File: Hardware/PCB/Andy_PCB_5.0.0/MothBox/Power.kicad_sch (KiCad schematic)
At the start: 28 parts, among them P1 Raw Input, P2 12V Regulated Input, P3 Input to regulator, Q1 BC817, Q2 TJ10S04M3L,LXHQ, U15 Place Holder voltage regulator, U19 INA219BIDCNT, U3 XL4015E1

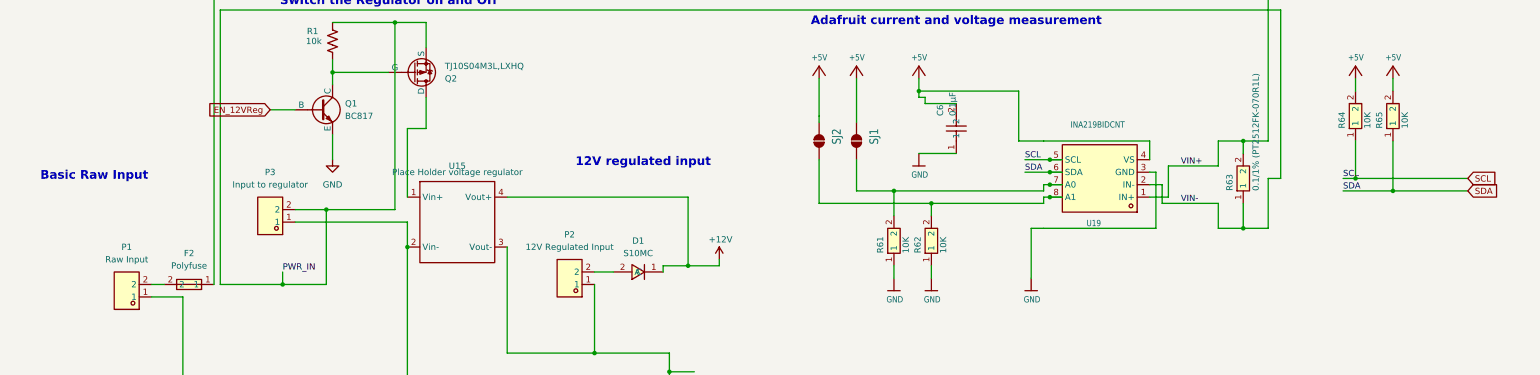
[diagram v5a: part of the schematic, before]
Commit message: added GPS 2 kinds
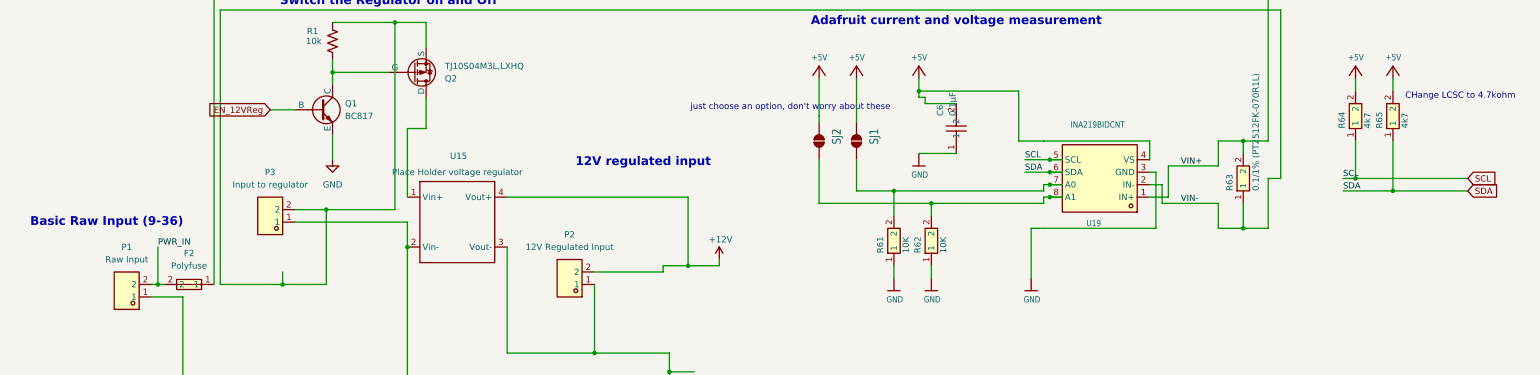
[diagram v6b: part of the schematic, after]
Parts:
- removed D1: S10MC, easyeda2kicad:SMC_L7.1-W6.2-LS8.1-RD, symbol easyeda2kicad:S10MC
- R64, R65: value 10K -> 4k7
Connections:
- net +12V: now also P2.2
- net PWR_IN: now also F2.2, P1.2; no longer P3.2, Q2.3 (S), R1.2, R63.1, U19.2 (IN-)
- new net VIN-: P3.2, Q2.3 (S), R1.2, R63.1, U19.2 (IN-)
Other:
- note added: "Basic Raw Input (9-36)"
- note added: "CHange LCSC to 4.7kohm"
- note added: "just choose an option, don't worry about these"
- note removed: "Basic Raw Input"
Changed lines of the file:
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@@
 		)
 	)
+	(text "CHange LCSC to 4.7kohm\n"
+		(exclude_from_sim no)
+		(at 317.246 35.306 0)
+		(effects
+			(font
+				(size 1.27 1.27)
+			)
+		)
+	)
+	(text "just choose an option, don't worry about these\n"
+		(exclude_from_sim no)
+		(at 180.848 37.592 0)
+		(effects
+			(font
+				(size 1.27 1.27)
+			)
+		)
+	)
 	(text "12V regulated input\n"
 		(exclude_from_sim no)
@@
 		)
 	)
-	(text "Basic Raw Input"
+	(text "Basic Raw Input (9-36)"
 		(exclude_from_sim no)
-		(at 39.116 51.562 0)
+		(at 41.656 60.96 0)
 		(effects
 			(font
@@
 	)
 	(junction
+		(at 52.07 73.66)
+		(diameter 0)
+		(color 0 0 0 0)
+	)
+	(junction
 		(at 140.97 87.63)
 		(diameter 0)
@@
 	(wire
 		(pts
+			(xy 50.8 73.66) (xy 52.07 73.66)
+		)
+		(stroke
+			(width 0)
+			(type default)
+		)
+	)
+	(wire
+		(pts
 			(xy 64.77 130.81) (xy 73.66 130.81)
 		)
@@
 	(wire
 		(pts
+			(xy 52.07 66.04) (xy 52.07 73.66)
+		)
+		(stroke
+			(width 0)
+			(type default)
+		)
+	)
+	(wire
+		(pts
 			(xy 254 55.88) (xy 257.81 55.88)
 		)
@@
 	(wire
 		(pts
-			(xy 140.97 71.12) (xy 144.78 71.12)
+			(xy 140.97 71.12) (xy 154.94 71.12)
 		)
 		(stroke
@@
 	(wire
 		(pts
-			(xy 50.8 73.66) (xy 53.34 73.66)
-		)
-		(stroke
-			(width 0)
-			(type default)
-		)
-	)
-	(wire
-		(pts
 			(xy 87.63 30.48) (xy 99.06 30.48)
 		)
@@
 	(wire
 		(pts
+			(xy 52.07 73.66) (xy 53.34 73.66)
+		)
+		(stroke
+			(width 0)
+			(type default)
+		)
+	)
+	(wire
+		(pts
 			(xy 146.05 128.27) (xy 146.05 120.65)
 		)
@@
 		)
 	)
-	(label "PWR_IN"
-		(at 77.47 71.12 0)
+	(label "FB"
+		(at 144.78 133.35 0)
 		(effects
 			(font
@@
 		)
 	)
-	(label "FB"
-		(at 144.78 133.35 0)
+	(label "SDA"
+		(at 228.6 50.8 0)
 		(effects
 			(font
-				(size 1.27 1.27)
+				(size 1.2446 1.2446)
 			)
 			(justify left bottom)
 		)
 	)
-	(label "SDA"
-		(at 228.6 50.8 0)
+	(label "PWR_IN"
+		(at 52.07 66.04 0)
 		(effects
 			(font
-				(size 1.2446 1.2446)
+				(size 1.27 1.27)
 			)
 			(justify left bottom)
@@
 			)
 		)
-		(property "Value" "10K"
+		(property "Value" "4k7"
 			(at 299.085 41.91 0)
 			(effects
@@
 	)
 	(symbol
-		(lib_id "easyeda2kicad:S10MC")
-		(at 149.86 71.12 180)
-		(unit 1)
-		(exclude_from_sim no)
-		(in_bom yes)
-		(on_board yes)
-		(dnp no)
-		(fields_autoplaced yes)
-		(property "Reference" "D1"
-			(at 149.86 64.77 0)
-			(effects
-				(font
-					(size 1.27 1.27)
-				)
-			)
-		)
-		(property "Value" "S10MC"
-			(at 149.86 67.31 0)
-			(effects
-				(font
-					(size 1.27 1.27)
-				)
-			)
-		)
-		(property "Footprint" "easyeda2kicad:SMC_L7.1-W6.2-LS8.1-RD"
-			(at 149.86 63.5 0)
-			(effects
-				(font
-					(size 1.27 1.27)
-				)
-				(hide yes)
-			)
-		)
-		(property "Datasheet" "https://lcsc.com/product-detail/Diodes-General-Purpose_S10MC_C169472.html"
-			(at 149.86 60.96 0)
-			(effects
-				(font
-					(size 1.27 1.27)
-				)
-				(hide yes)
-			)
-		)
-		(property "Description" ""
-			(at 149.86 71.12 0)
-			(effects
-				(font
-					(size 1.27 1.27)
-				)
-				(hide yes)
-			)
-		)
-		(property "LCSC Part" "C169472"
-			(at 149.86 58.42 0)
-			(effects
-				(font
-					(size 1.27 1.27)
-				)
-				(hide yes)
-			)
-		)
-		(pin "1"
-		)
-		(pin "2"
-		)
-		(instances
-			(project ""
-				(path "/9021e528-fc76-4423-a3f3-30f5652071cc/4a573100-9946-48c2-8ae5-35f893607623"
-					(reference "D1")
-					(unit 1)
-				)
-			)
-		)
-	)
-	(symbol
 		(lib_id "New_Library:Buck-Boost")
 		(at 113.03 60.96 0)
@@
 		(on_board no)
 		(dnp no)
-		(fields_autoplaced yes)
 		(property "Reference" "U15"
-			(at 113.03 49.53 0)
+			(at 113.284 47.498 0)
 			(effects
 				(font
@@
 			)
 		)
-		(property "Value" "10K"
+		(property "Value" "4k7"
 			(at 306.705 41.91 0)
 			(effects

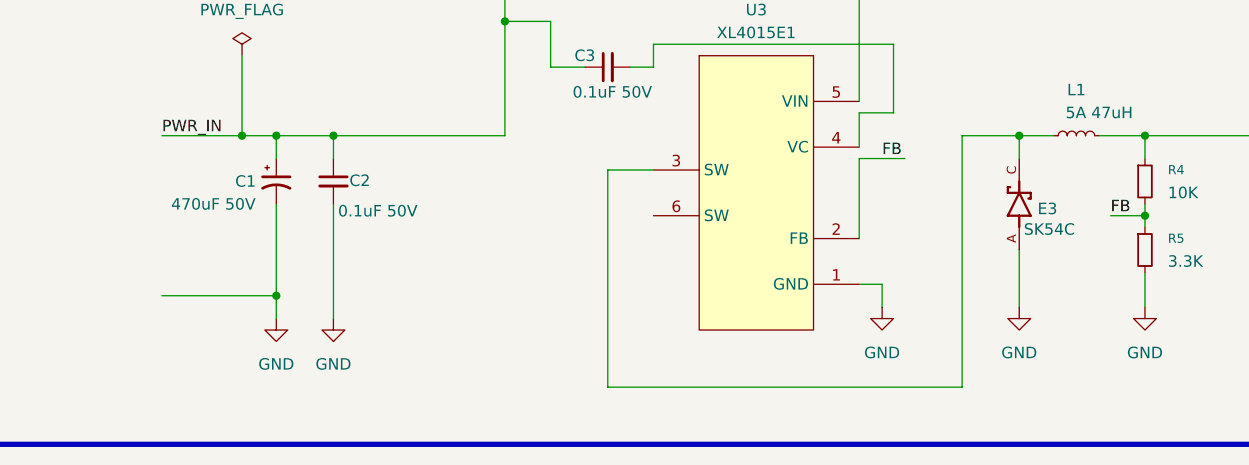
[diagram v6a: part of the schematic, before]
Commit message: Tweaked Mothbeam and added GPS footprints
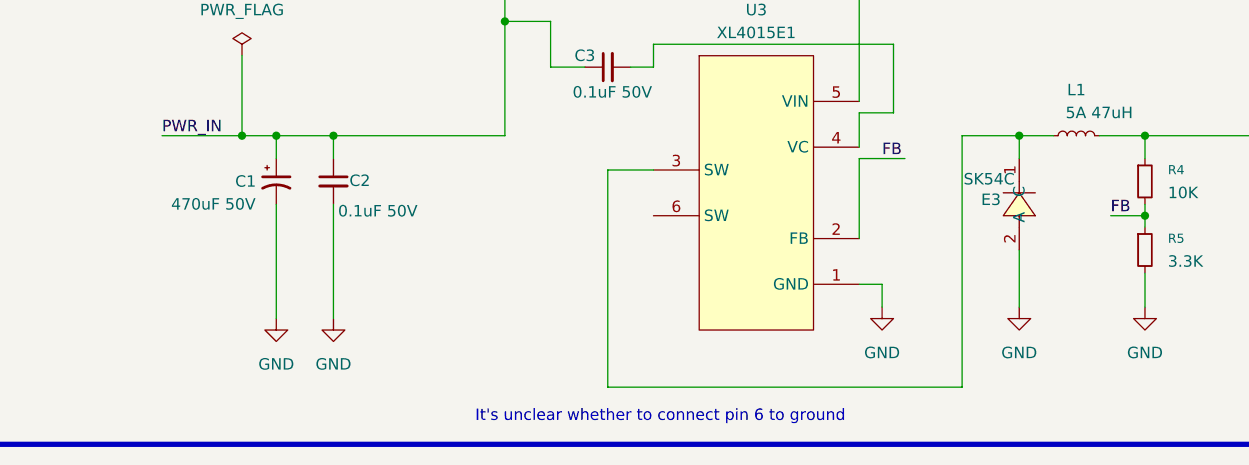
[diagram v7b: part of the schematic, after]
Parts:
- E3: footprint SK54C:DIO_SK54C -> easyeda2kicad:SMC_L6.9-W5.9-LS8.0-RD; symbol SK54C:SK54C -> easyeda2kicad:SK54C_C5449119; LCSC Part (none) -> C5449119
- P1, P2, P3: footprint easyeda2kicad:CONN-TH_DB301V-3.5-2P-GN -> easyeda2kicad:CONN-TH_2P-P5.08_DIBO_DB142R-5.08-2P; symbol easyeda2kicad:DB301V-3.5-2P-GN -> easyeda2kicad:DB142R-5.08-2P; LCSC Part C695629 -> C2898709
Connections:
- net GND: now also E3.2 (A); no longer E3.A
- net at L1.1, U3.3 (SW): now also E3.1 (C); no longer E3.C
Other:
- note added: "It's unclear whether to connect pin 6 to ground"
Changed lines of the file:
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@@
 		)
 	)
+	(text "It's unclear whether to connect pin 6 to ground\n"
+		(exclude_from_sim no)
+		(at 120.142 162.052 0)
+		(effects
+			(font
+				(size 1.27 1.27)
+				(color 255 20 18 1)
+			)
+		)
+	)
 	(text "CHange LCSC to 4.7kohm\n"
 		(exclude_from_sim no)
@@
 	)
 	(junction
-		(at 77.47 148.59)
-		(diameter 0)
-		(color 0 0 0 0)
-	)
-	(junction
 		(at 233.68 50.8)
 		(diameter 0)
@@
 	(wire
 		(pts
-			(xy 64.77 148.59) (xy 77.47 148.59)
-		)
-		(stroke
-			(width 0)
-			(type default)
-		)
-	)
-	(wire
-		(pts
 			(xy 278.13 13.97) (xy 278.13 44.45)
 		)
@@
 	(wire
 		(pts
-			(xy 77.47 138.43) (xy 77.47 148.59)
+			(xy 77.47 138.43) (xy 77.47 151.13)
 		)
 		(stroke
@@
 	(wire
 		(pts
-			(xy 77.47 148.59) (xy 77.47 151.13)
-		)
-		(stroke
-			(width 0)
-			(type default)
-		)
-	)
-	(wire
-		(pts
 			(xy 77.47 73.66) (xy 86.36 73.66)
 		)
@@
 	)
 	(symbol
-		(lib_id "easyeda2kicad:DB301V-3.5-2P-GN")
+		(lib_id "easyeda2kicad:DB142R-5.08-2P")
 		(at 135.89 72.39 180)
 		(unit 1)
@@
 			)
 		)
-		(property "Footprint" "easyeda2kicad:CONN-TH_DB301V-3.5-2P-GN"
+		(property "Footprint" "easyeda2kicad:CONN-TH_2P-P5.08_DIBO_DB142R-5.08-2P"
 			(at 135.89 63.5 0)
 			(effects
@@
 		)
 		(property "Datasheet" "https://lcsc.com/product-detail/Wire-To-Board-Wire-To-Wire-Connector_DIBO-DB301V-3-5-2P-GN_C695629.html"
-			(at 135.89 60.96 0)
+			(at 135.89 72.39 0)
 			(effects
 				(font
@@
 			)
 		)
-		(property "LCSC Part" "C695629"
-			(at 135.89 58.42 0)
+		(property "LCSC Part" "C2898709"
+			(at 135.89 60.96 0)
 			(effects
 				(font
@@
 	)
 	(symbol
-		(lib_id "easyeda2kicad:DB301V-3.5-2P-GN")
+		(lib_id "easyeda2kicad:DB142R-5.08-2P")
 		(at 74.93 59.69 180)
 		(unit 1)
@@
 			)
 		)
-		(property "Footprint" "easyeda2kicad:CONN-TH_DB301V-3.5-2P-GN"
+		(property "Footprint" "easyeda2kicad:CONN-TH_2P-P5.08_DIBO_DB142R-5.08-2P"
 			(at 74.93 50.8 0)
 			(effects
@@
 		)
 		(property "Datasheet" "https://lcsc.com/product-detail/Wire-To-Board-Wire-To-Wire-Connector_DIBO-DB301V-3-5-2P-GN_C695629.html"
-			(at 74.93 48.26 0)
+			(at 74.93 59.69 0)
 			(effects
 				(font
@@
 			)
 		)
-		(property "LCSC Part" "C695629"
-			(at 74.93 45.72 0)
+		(property "LCSC Part" "C2898709"
+			(at 74.93 48.26 0)
 			(effects
 				(font
@@
 	)
 	(symbol
-		(lib_id "SK54C:SK54C")
-		(at 160.02 138.43 90)
+		(lib_id "easyeda2kicad:SK54C_C5449119")
+		(at 160.02 138.43 270)
 		(unit 1)
 		(exclude_from_sim no)
@@
 		(dnp no)
 		(property "Reference" "E3"
-			(at 162.052 138.938 90)
+			(at 157.988 137.922 90)
 			(effects
 				(font
@@
 		)
 		(property "Value" "SK54C"
-			(at 160.528 141.224 90)
+			(at 159.512 135.636 90)
 			(effects
 				(font
@@
 			)
 		)
-		(property "Footprint" "SK54C:DIO_SK54C"
-			(at 160.02 138.43 0)
+		(property "Footprint" "easyeda2kicad:SMC_L6.9-W5.9-LS8.0-RD"
+			(at 152.4 138.43 0)
 			(effects
 				(font
 					(size 1.27 1.27)
 				)
-				(justify bottom)
 				(hide yes)
 			)
@@
 			)
 		)
-		(pin "A"
+		(property "LCSC Part" "C5449119"
+			(at 149.86 138.43 0)
+			(effects
+				(font
+					(size 1.27 1.27)
+				)
+				(hide yes)
+			)
 		)
-		(pin "C"
+		(pin "2"
+		)
+		(pin "1"
 		)
 		(instances
@@
 	)
 	(symbol
-		(lib_id "easyeda2kicad:DB301V-3.5-2P-GN")
+		(lib_id "easyeda2kicad:DB142R-5.08-2P")
 		(at 45.72 74.93 180)
 		(unit 1)
@@
 			)
 		)
-		(property "Footprint" "easyeda2kicad:CONN-TH_DB301V-3.5-2P-GN"
+		(property "Footprint" "easyeda2kicad:CONN-TH_2P-P5.08_DIBO_DB142R-5.08-2P"
 			(at 45.72 66.04 0)
 			(effects
@@
 		)
 		(property "Datasheet" "https://lcsc.com/product-detail/Wire-To-Board-Wire-To-Wire-Connector_DIBO-DB301V-3-5-2P-GN_C695629.html"
-			(at 45.72 63.5 0)
+			(at 45.72 74.93 0)
 			(effects
 				(font
@@
 			)
 		)
-		(property "LCSC Part" "C695629"
-			(at 45.72 60.96 0)
+		(property "LCSC Part" "C2898709"
+			(at 45.72 63.5 0)
 			(effects
 				(font

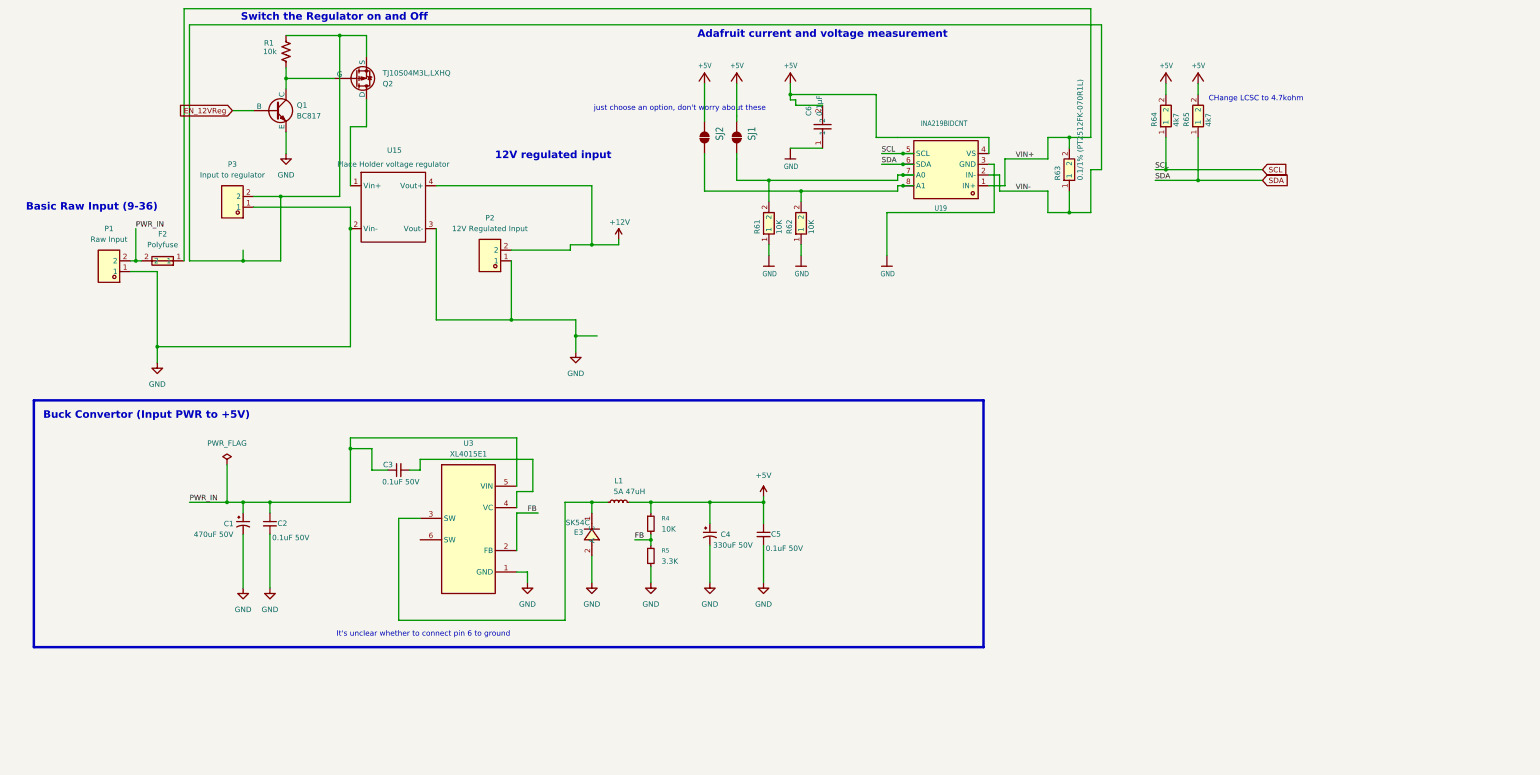
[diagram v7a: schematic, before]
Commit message: started adding test points, fixed current sensor should be 3.3v
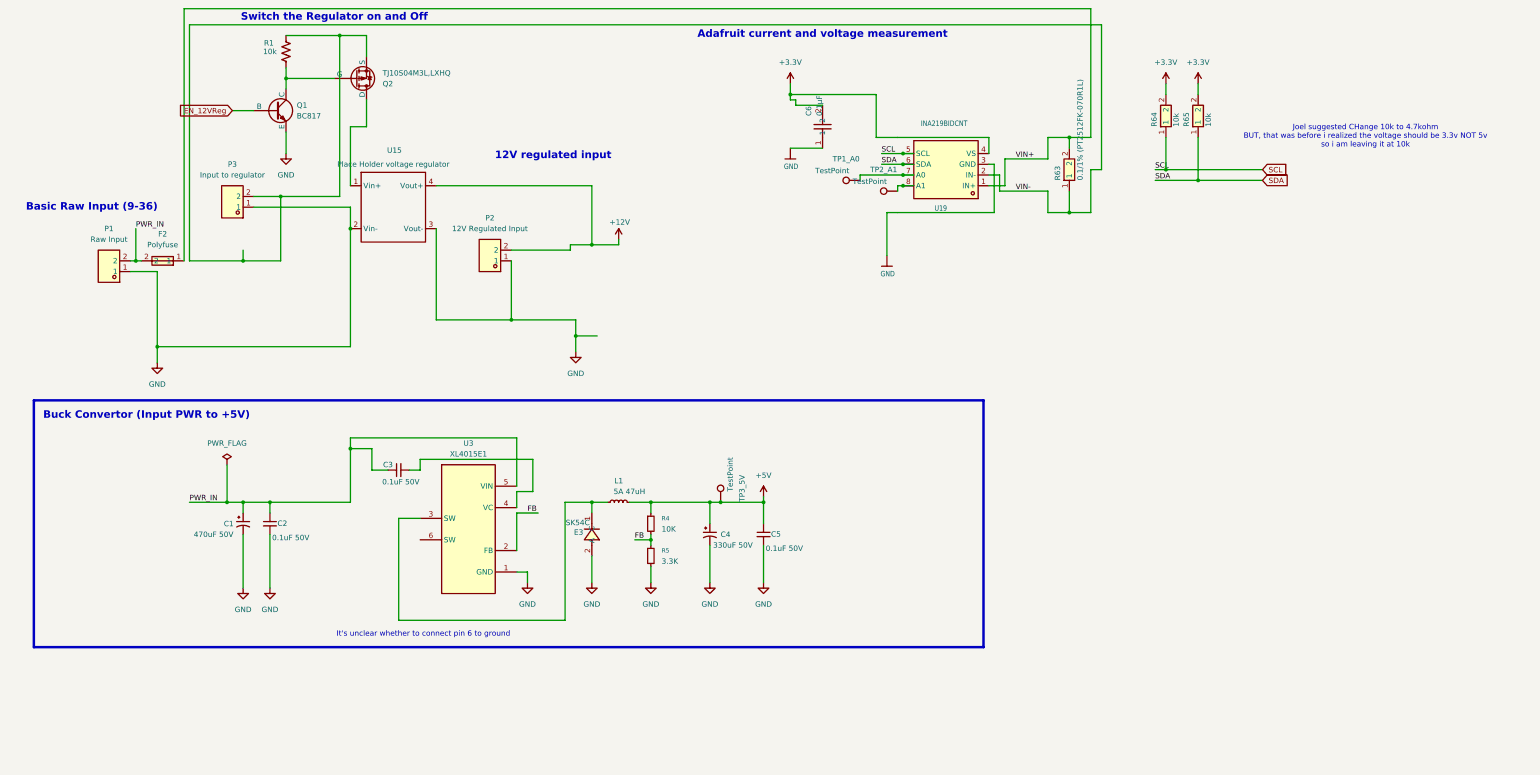
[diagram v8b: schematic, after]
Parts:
- removed R61, R62: 10K, easyeda2kicad:R0603, symbol easyeda2kicad:FRC0603J103TS
- removed SJ1: SOLDERJUMPERREFLOW_NOPASTE, Jumper:SolderJumper-2_P1.3mm_Open_RoundedPad1.0x1.5mm, symbol Jumper:SolderJumper_2_Open
- removed SJ2: SOLDERJUMPERREFLOW_NOPASTE, Jumper:SolderJumper-2_P1.3mm_Open_TrianglePad1.0x1.5mm, symbol Jumper:SolderJumper_2_Open
- added TP1_A0, TP2_A1, TP3_5V: TestPoint, TestPoint:TestPoint_THTPad_D1.0mm_Drill0.5mm, symbol Connector:TestPoint
- R64, R65: value 4k7 -> 10k
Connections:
- net +5V: now also TP3_5V.1; no longer C6.2, R64.2, R65.2, U19.4 (VS)
- net at U19.8 (A1): now also TP2_A1.1
- net at U19.7 (A0): now also TP1_A0.1
- new net +3.3V: C6.2, R64.2, R65.2, U19.4 (VS)
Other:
- note added: "Joel suggested CHange 10k to 4.7kohm BUT, that was before i realized the voltage should be 3.3v NOT 5v so i am leaving it at 10k"
- note removed: "CHange LCSC to 4.7kohm"
- note removed: "just choose an option, don't worry about these"
